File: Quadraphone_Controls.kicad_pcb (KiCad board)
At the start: 2 copper layers, 60 x 110 mm, 17 parts, among them J1 Conn_01x10_Female, J10 Pitch_In, J11 Mix_Out, J2 Conn_01x10_Female, J3 Conn_01x10_Female, J4 Conn_01x10_Female, J5 PWM_CV, J6 LFO_IN, J7 PWM_CV_In, J8 Synch_Signal_In, J9 Freq_Mod_In, SW1 Synch_Type, SW2 Output_Type

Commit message: Started laying out Panel
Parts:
- moved SW2 32.5 mm to (63.5, 79.5)
- moved SW1 14.5 mm to (96.5, 77.0)
- moved Vibrato_Depth1 13.0 mm to (80.0, 79.5)
- moved J7 6.37 mm to (80.0, 125.1)
- moved J8 6.37 mm to (97.0, 125.1)
- moved J9 6.37 mm to (63.0, 125.1)
- moved J11 6.30 mm to (91.0, 144.0)
- moved J10 6.23 mm to (68.9, 144.0)
- moved Octave_Tune1 1.20 mm to (65.8, 57.5)
- moved Fine_Tune1 0.80 mm to (94.2, 57.5)
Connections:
- Fine_Tune1 pad 3: +2V5 -> +5V
- J3 pad 10: /OCT_TUNE -> /FINE_TUNE
- J4 pad 8: /FINE_TUNE -> /OCT_TUNE
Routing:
- net /MIX_OUT2: track 0.00 -> 121.6 mm
- net /MIX_OUT1: track 0.00 -> 116.4 mm
- net /FINE_TUNE: track 0.00 -> 84.6 mm
- net /OCT_TUNE: track 0.00 -> 82.2 mm
- net +5V: track 0.00 -> 73.4 mm
- net /V_PER_OCT2: track 0.00 -> 73.3 mm
- net /V_PER_OCT1: track 0.00 -> 73.1 mm
- net /FREQ_MOD3: track 0.00 -> 71.5 mm
- net /SOFT_SYNCH_SW: track 0.00 -> 69.1 mm
- net /SYNCH_SIGNAL2: track 0.00 -> 68.3 mm
- net /SAW_SW: track 0.00 -> 65.9 mm
- net +12V: track 0.00 -> 59.4 mm
- net /FREQ_MOD1: track 0.00 -> 59.0 mm
- net -12V: track 0.00 -> 58.2 mm
- net /SYNCH_SIGNAL4: track 0.00 -> 50.7 mm
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- added copper zone on B.Cu, net GND
- added copper zone on F.Cu, net GND
- removed copper zone on B.Cu, net (none)
- removed copper zone on F.Cu, net (none)

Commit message: Rough Layout of Panel
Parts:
- moved J8 0.82 mm to (97.8, 124.9)
- moved J9 0.82 mm to (62.2, 124.9)
- moved J7 0.20 mm to (80.0, 124.9)
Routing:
- net /FREQ_MOD2: track 39.0 -> 38.0 mm
- net /SYNCH_SIGNAL4: track 50.7 -> 51.6 mm
- net /FREQ_MOD1: track 59.0 -> 59.8 mm
- net /FREQ_MOD4: track 23.5 -> 24.0 mm
- net /FREQ_MOD3: track 71.5 -> 72.0 mm

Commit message: First draft panel done
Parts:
- moved J5 31.1 mm to (80.0, 125.0)
- moved J6 22.6 mm to (80.0, 109.0)
- moved Vibrato_Depth1 21.6 mm to (64.0, 94.0)
- moved J8 21.1 mm to (98.4, 146.0)
- moved PWM_Pot1 17.9 mm to (96.0, 94.0)
- moved J7 16.5 mm to (96.0, 121.0)
- moved J11 11.2 mm to (80.0, 146.0)
- moved J10 7.57 mm to (61.6, 146.0)
- moved SW1 4.34 mm to (94.0, 73.5)
- moved SW2 4.30 mm to (66.0, 76.0)
- moved J9 4.30 mm to (64.0, 121.0)
- moved Fine_Tune1 0.54 mm to (94.0, 57.0)
- moved Octave_Tune1 0.54 mm to (66.0, 57.0)
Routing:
- net /SYNCH_SIGNAL2: track 68.5 -> 96.4 mm
- net /SYNCH_SIGNAL1: track 45.5 -> 67.3 mm
- net /LIN_FREQ_IN: track 44.3 -> 23.1 mm
- net /LFO_IN: track 38.5 -> 18.6 mm
- net -12V: track 58.2 -> 42.6 mm
- net /PWM_CV: track 15.3 -> 30.2 mm
- net /PWM_CV4: track 31.0 -> 45.6 mm
- net /V_PER_OCT3: track 48.2 -> 62.4 mm
- net /PWM_CV3: track 42.4 -> 28.3 mm
- net /MIX_OUT3: track 44.2 -> 57.6 mm
- net /MIX_OUT2: track 121.6 -> 108.3 mm
- net /MIX_OUT4: track 48.8 -> 36.2 mm, vias 1 -> 0
- net /PWM_CV2: track 50.2 -> 61.0 mm
- net /PWM_CV1: track 49.9 -> 39.2 mm
- net /MIX_OUT1: track 116.4 -> 126.0 mm
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
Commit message: Refinements to panel and controls
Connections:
- Fine_Tune1 pad 1: GND -> +5V
- Fine_Tune1 pad 3: +5V -> GND
- Octave_Tune1 pad 1: GND -> +5V
- Octave_Tune1 pad 3: +5V -> GND
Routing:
- net +5V: track 67.4 -> 86.1 mm
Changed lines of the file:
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@@
       (net 4 "/PWM_CV1") (pintype "passive"))
     (pad "5" thru_hole circle (at 0.68 -4.65) (size 1.5 1.5) (drill 0.9) (layers *.Cu *.Mask)
-      (net 38 "unconnected-(J7-Pad5)") (pintype "passive"))
+      (net 38 "unconnected-(J7-Pad5)") (pintype "passive+no_connect"))
     (pad "6" thru_hole circle (at 1.95 -7.19) (size 1.5 1.5) (drill 0.9) (layers *.Cu *.Mask)
-      (net 39 "unconnected-(J7-Pad6)") (pintype "passive"))
+      (net 39 "unconnected-(J7-Pad6)") (pintype "passive+no_connect"))
     (pad "7" thru_hole circle (at 3.22 -4.65) (size 1.5 1.5) (drill 0.9) (layers *.Cu *.Mask)
-      (net 40 "unconnected-(J7-Pad7)") (pintype "passive"))
+      (net 40 "unconnected-(J7-Pad7)") (pintype "passive+no_connect"))
     (pad "8" thru_hole circle (at 4.49 -7.19) (size 1.5 1.5) (drill 0.9) (layers *.Cu *.Mask)
-      (net 41 "unconnected-(J7-Pad8)") (pintype "passive"))
+      (net 41 "unconnected-(J7-Pad8)") (pintype "passive+no_connect"))
     (model "${CUSTOM_3D}/428788506.stp"
       (offset (xyz 0.06 -0.3 6.5))
@@
     (pad "" np_thru_hole circle locked (at 4.4 0.5 90) (size 4 4) (drill 2) (layers *.Cu *.Mask))
     (pad "1" thru_hole circle locked (at 2.5 7.5 90) (size 1.8 1.8) (drill 1) (layers *.Cu *.Mask)
-      (net 24 "GND") (pinfunction "1") (pintype "passive"))
+      (net 27 "+5V") (pinfunction "1") (pintype "passive"))
     (pad "2" thru_hole circle locked (at 0 7.5 90) (size 1.8 1.8) (drill 1) (layers *.Cu *.Mask)
       (net 36 "/FINE_TUNE") (pinfunction "2") (pintype "passive"))
     (pad "3" thru_hole circle locked (at -2.5 7.5 90) (size 1.8 1.8) (drill 1) (layers *.Cu *.Mask)
-      (net 27 "+5V") (pinfunction "3") (pintype "passive"))
+      (net 24 "GND") (pinfunction "3") (pintype "passive"))
     (model "${CUSTOM_3D}/ALPHA-RD901F-40.step"
       (offset (xyz -0 -0.2 0))
@@
       (net 16 "/FREQ_MOD1") (pintype "passive"))
     (pad "5" thru_hole circle (at 0.68 -4.65) (size 1.5 1.5) (drill 0.9) (layers *.Cu *.Mask)
-      (net 46 "unconnected-(J9-Pad5)") (pintype "passive"))
+      (net 46 "unconnected-(J9-Pad5)") (pintype "passive+no_connect"))
     (pad "6" thru_hole circle (at 1.95 -7.19) (size 1.5 1.5) (drill 0.9) (layers *.Cu *.Mask)
-      (net 47 "unconnected-(J9-Pad6)") (pintype "passive"))
+      (net 47 "unconnected-(J9-Pad6)") (pintype "passive+no_connect"))
     (pad "7" thru_hole circle (at 3.22 -4.65) (size 1.5 1.5) (drill 0.9) (layers *.Cu *.Mask)
-      (net 48 "unconnected-(J9-Pad7)") (pintype "passive"))
+      (net 48 "unconnected-(J9-Pad7)") (pintype "passive+no_connect"))
     (pad "8" thru_hole circle (at 4.49 -7.19) (size 1.5 1.5) (drill 0.9) (layers *.Cu *.Mask)
-      (net 49 "unconnected-(J9-Pad8)") (pintype "passive"))
+      (net 49 "unconnected-(J9-Pad8)") (pintype "passive+no_connect"))
     (model "${CUSTOM_3D}/428788506.stp"
       (offset (xyz 0.06 -0.3 6.5))
@@
     (pad "" np_thru_hole circle locked (at 4.4 0.5 90) (size 4 4) (drill 2) (layers *.Cu *.Mask))
     (pad "1" thru_hole circle locked (at 2.5 7.5 90) (size 1.8 1.8) (drill 1) (layers *.Cu *.Mask)
-      (net 24 "GND") (pinfunction "1") (pintype "passive"))
+      (net 27 "+5V") (pinfunction "1") (pintype "passive"))
     (pad "2" thru_hole circle locked (at 0 7.5 90) (size 1.8 1.8) (drill 1) (layers *.Cu *.Mask)
       (net 32 "/OCT_TUNE") (pinfunction "2") (pintype "passive"))
     (pad "3" thru_hole circle locked (at -2.5 7.5 90) (size 1.8 1.8) (drill 1) (layers *.Cu *.Mask)
-      (net 27 "+5V") (pinfunction "3") (pintype "passive"))
+      (net 24 "GND") (pinfunction "3") (pintype "passive"))
     (model "${CUSTOM_3D}/ALPHA-RD901F-40.step"
       (offset (xyz -0 -0.2 0))
@@
       (net 12 "/SYNCH_SIGNAL1") (pintype "passive"))
     (pad "5" thru_hole circle (at 0.68 -4.65) (size 1.5 1.5) (drill 0.9) (layers *.Cu *.Mask)
-      (net 42 "unconnected-(J8-Pad5)") (pintype "passive"))
+      (net 42 "unconnected-(J8-Pad5)") (pintype "passive+no_connect"))
     (pad "6" thru_hole circle (at 1.95 -7.19) (size 1.5 1.5) (drill 0.9) (layers *.Cu *.Mask)
-      (net 43 "unconnected-(J8-Pad6)") (pintype "passive"))
+      (net 43 "unconnected-(J8-Pad6)") (pintype "passive+no_connect"))
     (pad "7" thru_hole circle (at 3.22 -4.65) (size 1.5 1.5) (drill 0.9) (layers *.Cu *.Mask)
-      (net 44 "unconnected-(J8-Pad7)") (pintype "passive"))
+      (net 44 "unconnected-(J8-Pad7)") (pintype "passive+no_connect"))
     (pad "8" thru_hole circle (at 4.49 -7.19) (size 1.5 1.5) (drill 0.9) (layers *.Cu *.Mask)
-      (net 45 "unconnected-(J8-Pad8)") (pintype "passive"))
+      (net 45 "unconnected-(J8-Pad8)") (pintype "passive+no_connect"))
     (model "${CUSTOM_3D}/428788506.stp"
       (offset (xyz 0.06 -0.3 6.5))
@@
       (effects (font (size 1 1) (thickness 0.15)))
     )
-    (fp_text value "10k" (at -0.2 -7.4) (layer "F.Fab")
+    (fp_text value "10k" (at 0 -6.9) (layer "F.Fab")
       (effects (font (size 1 1) (thickness 0.15)))
     )
@@
       (net 8 "/MIX_OUT1") (pintype "passive"))
     (pad "5" thru_hole circle (at 0.68 -4.65) (size 1.5 1.5) (drill 0.9) (layers *.Cu *.Mask)
-      (net 54 "unconnected-(J11-Pad5)") (pintype "passive"))
+      (net 54 "unconnected-(J11-Pad5)") (pintype "passive+no_connect"))
     (pad "6" thru_hole circle (at 1.95 -7.19) (size 1.5 1.5) (drill 0.9) (layers *.Cu *.Mask)
-      (net 53 "unconnected-(J11-Pad6)") (pintype "passive"))
+      (net 53 "unconnected-(J11-Pad6)") (pintype "passive+no_connect"))
     (pad "7" thru_hole circle (at 3.22 -4.65) (size 1.5 1.5) (drill 0.9) (layers *.Cu *.Mask)
-      (net 52 "unconnected-(J11-Pad7)") (pintype "passive"))
+      (net 52 "unconnected-(J11-Pad7)") (pintype "passive+no_connect"))
     (pad "8" thru_hole circle (at 4.49 -7.19) (size 1.5 1.5) (drill 0.9) (layers *.Cu *.Mask)
-      (net 51 "unconnected-(J11-Pad8)") (pintype "passive"))
+      (net 51 "unconnected-(J11-Pad8)") (pintype "passive+no_connect"))
     (model "${CUSTOM_3D}/428788506.stp"
       (offset (xyz 0.06 -0.3 6.5))
@@
   (segment (start 59.6 69.8) (end 59.6 70.9) (width 0.25) (layer "F.Cu") (net 26))
   (segment (start 66 75) (end 66 77) (width 0.25) (layer "F.Cu") (net 26))
+  (segment (start 66 73.585) (end 68.415 76) (width 0.25) (layer "F.Cu") (net 27))
+  (segment (start 68.5 64.5) (end 66 67) (width 0.25) (layer "F.Cu") (net 27))
   (segment (start 66 67) (end 66 73.585) (width 0.25) (layer "F.Cu") (net 27))
-  (segment (start 63.5 64.5) (end 66 67) (width 0.25) (layer "F.Cu") (net 27))
-  (segment (start 66 73.585) (end 68.415 76) (width 0.25) (layer "F.Cu") (net 27))
-  (segment (start 65.3 63) (end 63.3 65) (width 0.25) (layer "F.Cu") (net 27))
-  (segment (start 90 63) (end 65.3 63) (width 0.25) (layer "F.Cu") (net 27))
-  (segment (start 91.5 64.5) (end 90 63) (width 0.25) (layer "F.Cu") (net 27))
-  (segment (start 92.2939 75.9939) (end 91.5 75.2) (width 0.25) (layer "F.Cu") (net 27))
-  (segment (start 91.5 75.2) (end 91.5 64.5) (width 0.25) (layer "F.Cu") (net 27))
-  (segment (start 94 75.9939) (end 92.2939 75.9939) (width 0.25) (layer "F.Cu") (net 27))
-  (segment (start 52.8 65.54) (end 62.76 65.54) (width 0.25) (layer "B.Cu") (net 27))
-  (segment (start 62.76 65.54) (end 63.3 65) (width 0.25) (layer "B.Cu") (net 27))
+  (segment (start 70 63) (end 95 63) (width 0.25) (layer "B.Cu") (net 27))
+  (segment (start 52.8 65.54) (end 58.76 65.54) (width 0.25) (layer "B.Cu") (net 27))
+  (segment (start 58.76 65.54) (end 61.7 62.6) (width 0.25) (layer "B.Cu") (net 27))
+  (segment (start 68.5 64.5) (end 70 63) (width 0.25) (layer "B.Cu") (net 27))
+  (segment (start 95 63) (end 96.5 64.5) (width 0.25) (layer "B.Cu") (net 27))
+  (segment (start 94 75.9939) (end 68.4211 75.9939) (width 0.25) (layer "B.Cu") (net 27))
+  (segment (start 68.4211 75.9939) (end 68.415 76) (width 0.25) (layer "B.Cu") (net 27))
+  (segment (start 61.7 62.6) (end 66.6 62.6) (width 0.25) (layer "B.Cu") (net 27))
+  (segment (start 66.6 62.6) (end 68.5 64.5) (width 0.25) (layer "B.Cu") (net 27))
   (segment (start 66.115 78.4) (end 61.5 78.4) (width 0.25) (layer "F.Cu") (net 29))
   (segment (start 61.5 78.4) (end 56.26 73.16) (width 0.25) (layer "F.Cu") (net 29))

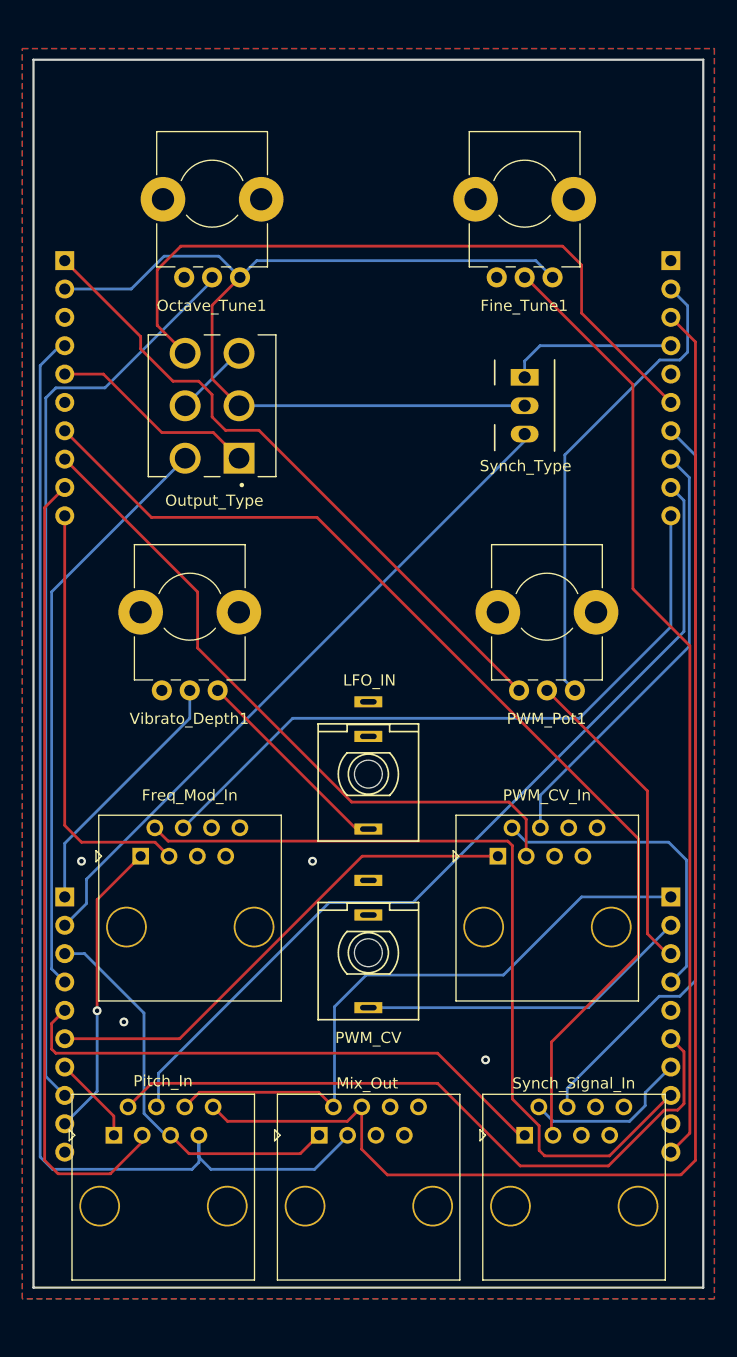
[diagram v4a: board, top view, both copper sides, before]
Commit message: Fixed ground connections on component board
Added JLC PCB plug-in
Schematic clean-up
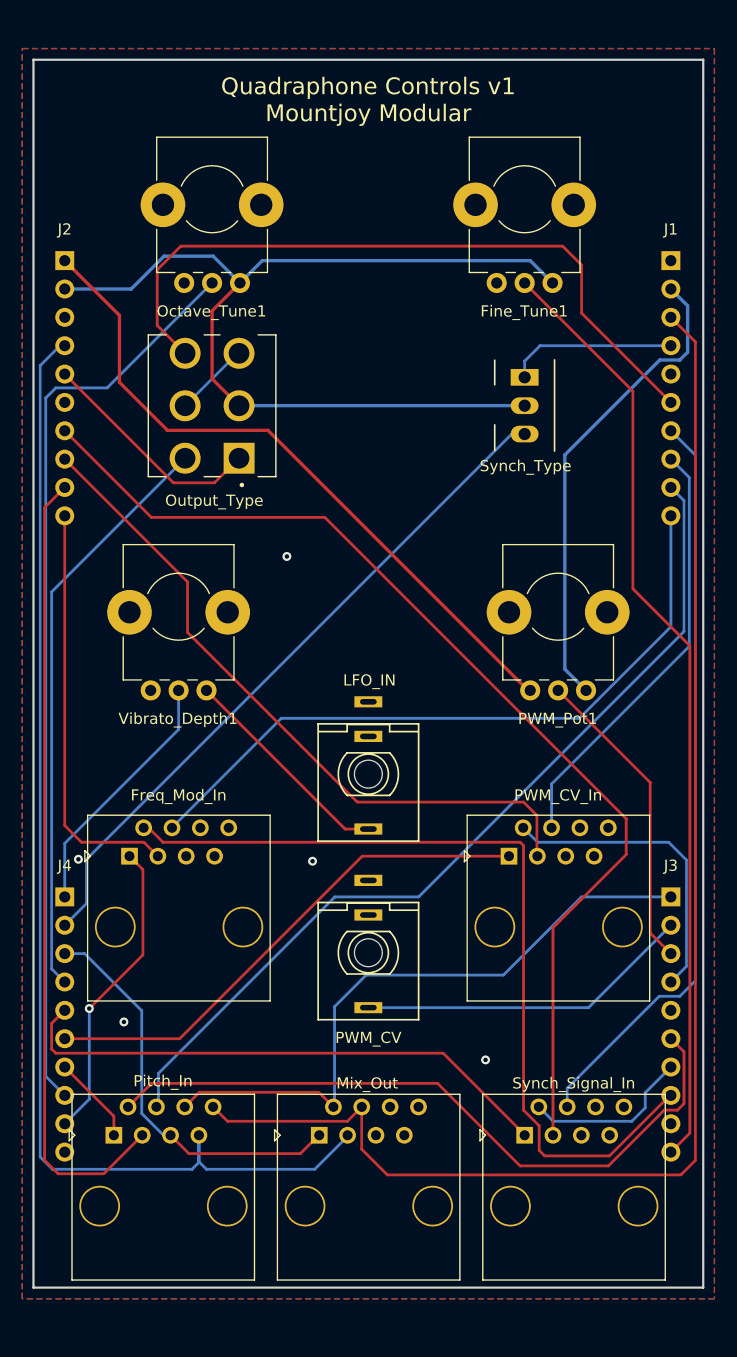
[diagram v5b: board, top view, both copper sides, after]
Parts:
- moved J7 1.00 mm to (97.0, 121.0)
- moved J9 1.00 mm to (63.0, 121.0)
- moved PWM_Pot1 1.00 mm to (97.0, 94.0)
- moved Vibrato_Depth1 1.00 mm to (63.0, 94.0)
- moved Fine_Tune1 0.50 mm to (94.0, 57.5)
- moved Octave_Tune1 0.50 mm to (66.0, 57.5)
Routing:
- net +12V: track 58.5 -> 61.2 mm
- net /PULSE_SW: track 18.7 -> 20.6 mm
- net /FREQ_MOD3: track 75.2 -> 76.8 mm
- net /FREQ_MOD1: track 61.1 -> 62.1 mm
- net /PWM_CV4: track 45.6 -> 46.6 mm
- net /LFO_IN: track 18.6 -> 19.6 mm
- net /FREQ_MOD2: track 38.2 -> 37.2 mm
- net /PWM_CV3: track 28.3 -> 27.3 mm
- net /PWM_CV2: track 61.0 -> 61.8 mm
- net /SOFT_SYNCH_SW: track 61.1 -> 61.7 mm
- net /SYNCH_SIGNAL2: track 96.4 -> 95.8 mm
- net /PWM_POT: track 28.4 -> 27.8 mm
- net /FREQ_MOD4: track 26.8 -> 27.4 mm
- net /FINE_TUNE: track 85.3 -> 84.7 mm
- net GND: vias 4 -> 5
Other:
- board text added: "J1"
- board text added: "J2"
- board text added: "J3"
- board text added: "J4"
- board text added: "Quadraphone Controls v1 Mountjoy Modular"
